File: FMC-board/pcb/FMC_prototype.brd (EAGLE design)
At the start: 76.5 x 69 mm, 71 parts, among them U1 4901, U2 TPS79333, U3 ADN4663, U4 ADN4663, U5 ADN4664, U6 PDS1-S12-S5-S, U8 4901

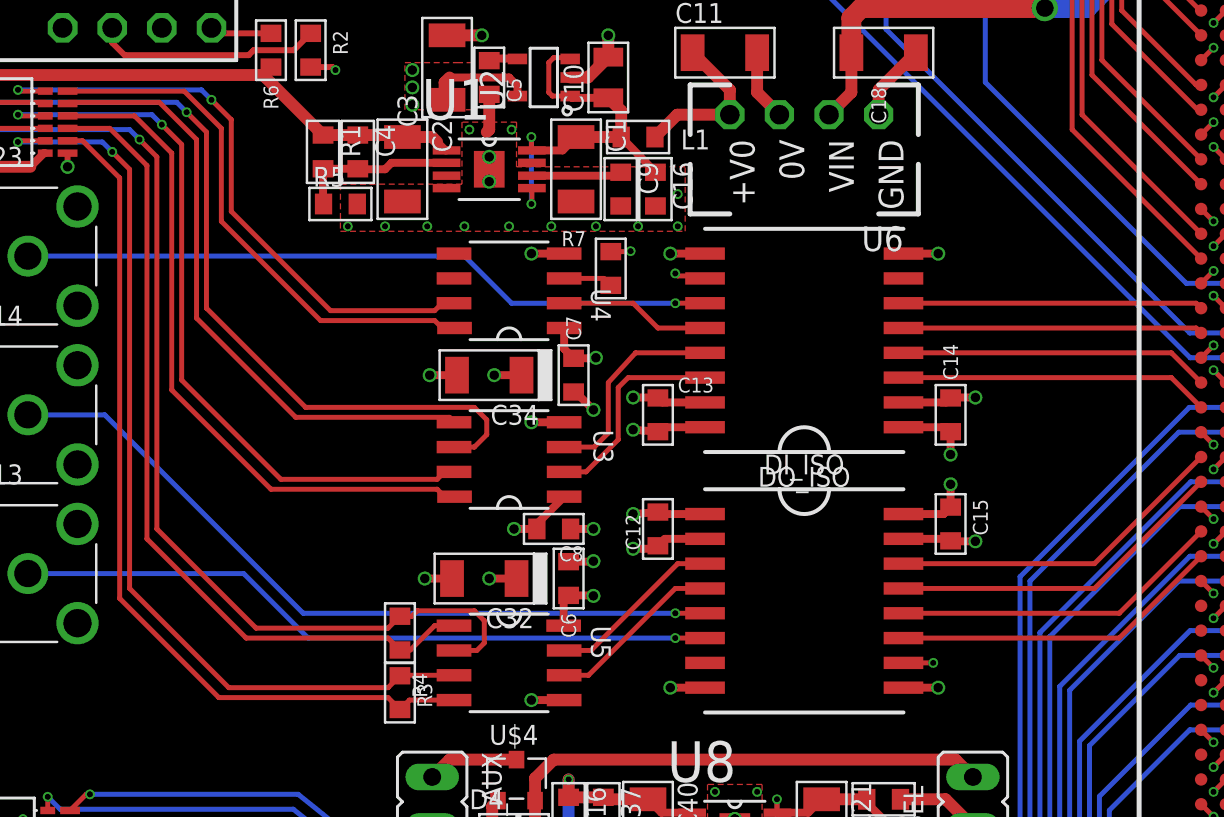
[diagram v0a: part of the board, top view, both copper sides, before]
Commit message: tightened routing a bit & added 3v3 test point
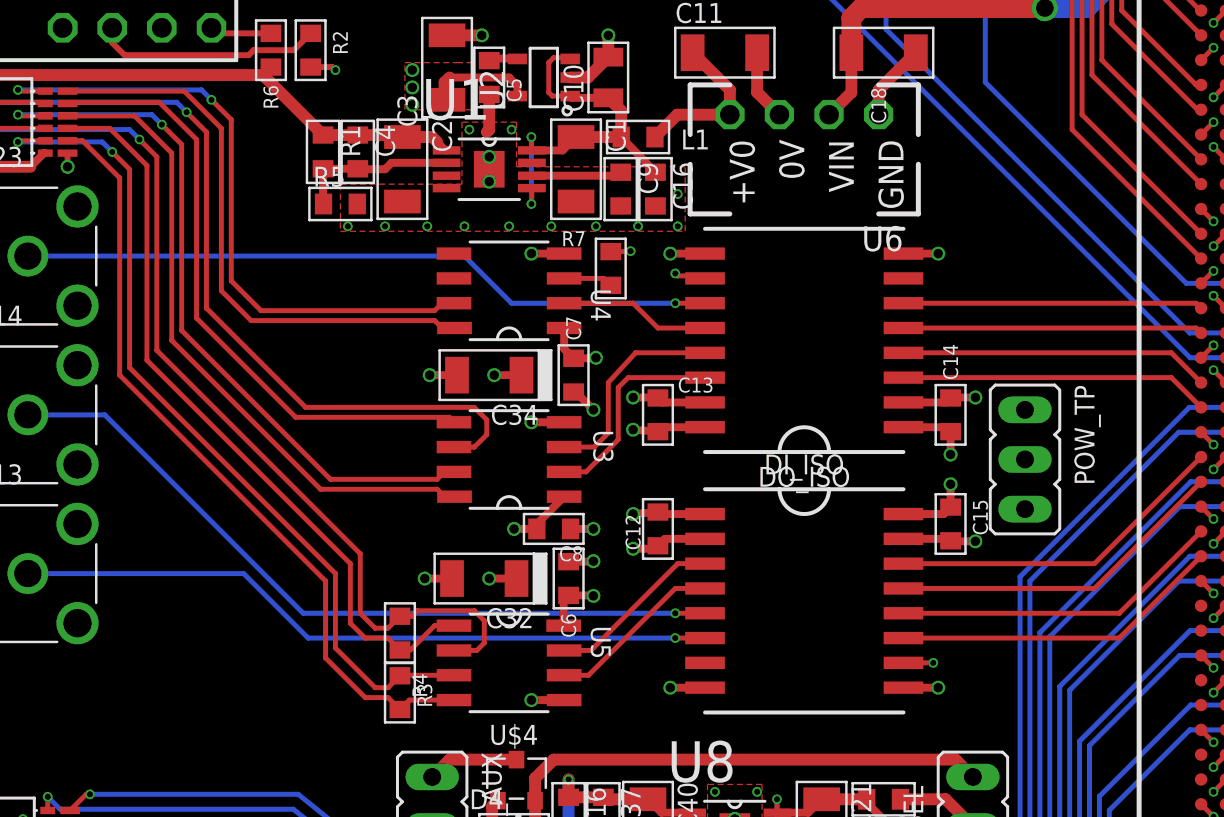
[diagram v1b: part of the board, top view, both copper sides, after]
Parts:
- added POW_TP: (no value), jonnew:JP3
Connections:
- new net N$11: POW_TP.2
- net +3V3: now also POW_TP.1
- net GND: now also POW_TP.3
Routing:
- net MISO2-_ISOLATED: track 44.9 -> 40.5 mm
- net MISO2+_ISOLATED: track 48.4 -> 44.0 mm
- net MISO1+_ISOLATED: track 53.5 -> 50.0 mm
- net MISO1-_ISOLATED: track 42.6 -> 39.0 mm
- net CS+_ISOLATED: track 31.3 -> 33.4 mm
- net CS-_ISOLATED: track 27.6 -> 29.7 mm
- net N$13: track 35.0 -> 33.5 mm
- net N$12: track 38.7 -> 37.2 mm

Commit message: connected FMC mount holes to non-isolated gnd
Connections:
- net GND: now also U$2.BEZ1, U$2.BEZ2
- net GND_ISO: no longer U$2.BEZ1, U$2.BEZ2
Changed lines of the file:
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@@
 <wire x1="3.175" y1="49.3014" x2="2.159" y2="49.3014" width="0.254" layer="16"/>
 <contactref element="POW_TP" pad="3"/>
+<contactref element="U$2" pad="BEZ2"/>
+<contactref element="U$2" pad="BEZ1"/>
 </signal>
 <signal name="MISO1_ISO">
@@
 <contactref element="H14" pad="GND$2"/>
 <contactref element="C11" pad="2"/>
-<contactref element="U$2" pad="BEZ2"/>
-<contactref element="U$2" pad="BEZ1"/>
 <polygon width="0.4064" layer="2" isolate="0.254">
 <vertex x="-67.31" y="13.589"/>
@@
 <wire x1="-30.3784" y1="37.5666" x2="-30.353" y2="37.592" width="0.254" layer="1"/>
 <wire x1="-33.7566" y1="37.465" x2="-35.433" y2="37.465" width="0.4064" layer="1"/>
-<wire x1="-58.674" y1="18.542" x2="-54.6" y2="2.5" width="0" layer="19" extent="1-1"/>
-<wire x1="-54.6" y1="59.05" x2="-54.356" y2="49.022" width="0" layer="19" extent="1-1"/>
 </signal>
 <signal name="+3V6_ISO">

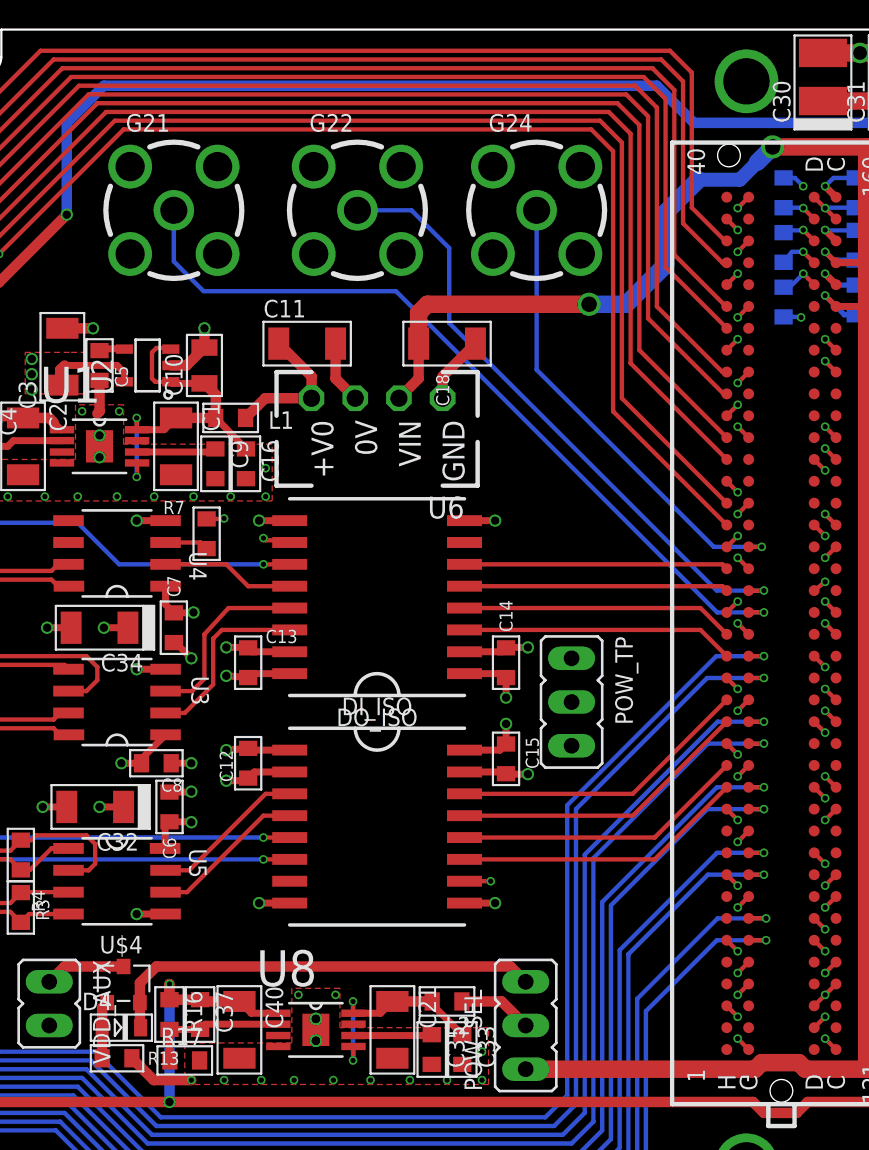
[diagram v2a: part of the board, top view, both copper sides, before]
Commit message: added schottky diodes for FPGA input protection
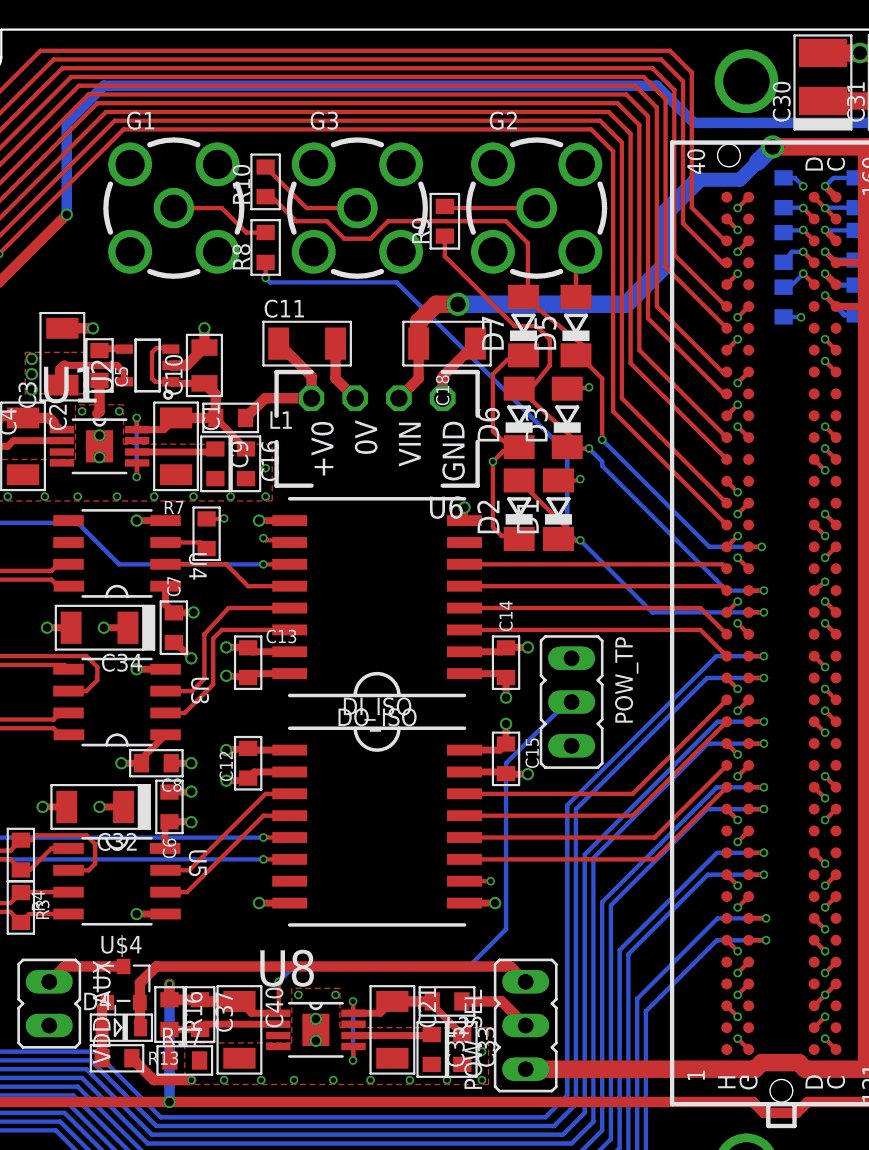
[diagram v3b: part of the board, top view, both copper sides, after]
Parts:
- removed G21, G22, G24: 142-0701, jonnew:SMA_JACK_142-0701-201
- added D1, D2, D3, D5, D6, D7: PMLL4150, diode:SOD80C
- added G1, G2, G3: 142-0701, jonnew:SMA_JACK_142-0701-201
- added R10, R8, R9: 100, jonnew:0603
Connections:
- removed net N$11: POW_TP.2
- new net N$18: G2.CLK, R9.2
- new net N$19: G3.CLK, R10.2
- new net N$2: G1.CLK, R8.2
- net +3V3: now also D2.C, D6.C, D7.C
- net +3V6: now also POW_TP.2
- net G21: now also D1.C, D2.A, R8.1; no longer G21.CLK
- net G22: now also D3.C, D6.A, R9.1; no longer G22.CLK
- net G24: now also D5.C, D7.A, R10.1; no longer G24.CLK
- net GND: now also D1.A, D3.A, D5.A, G1.GND$1, G1.GND$2, G1.GND$3, G1.GND$4, G2.GND$1, G2.GND$2, G2.GND$3, G2.GND$4, G3.GND$1, G3.GND$2, G3.GND$3, G3.GND$4; no longer G21.GND$1, G21.GND$2, G21.GND$3, G21.GND$4, G22.GND$1, G22.GND$2, G22.GND$3, G22.GND$4, G24.GND$1, G24.GND$2, G24.GND$3, G24.GND$4
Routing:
- net +3V6: track 220.3 -> 251.6 mm, vias 4 -> 5
- net G24: track 27.4 -> 43.9 mm, vias 1 -> 2
- net +3V3: track 18.3 -> 34.4 mm, vias 7 -> 8
- net N$19: track 0.00 -> 6.32 mm
- net N$2: track 0.00 -> 5.92 mm
- net N$18: track 0.00 -> 5.38 mm
- net GND: track 90.1 -> 94.9 mm
- net G21: track 46.6 -> 47.9 mm, vias 1 -> 3
- net G22: track 36.2 -> 35.1 mm, vias 1 -> 2

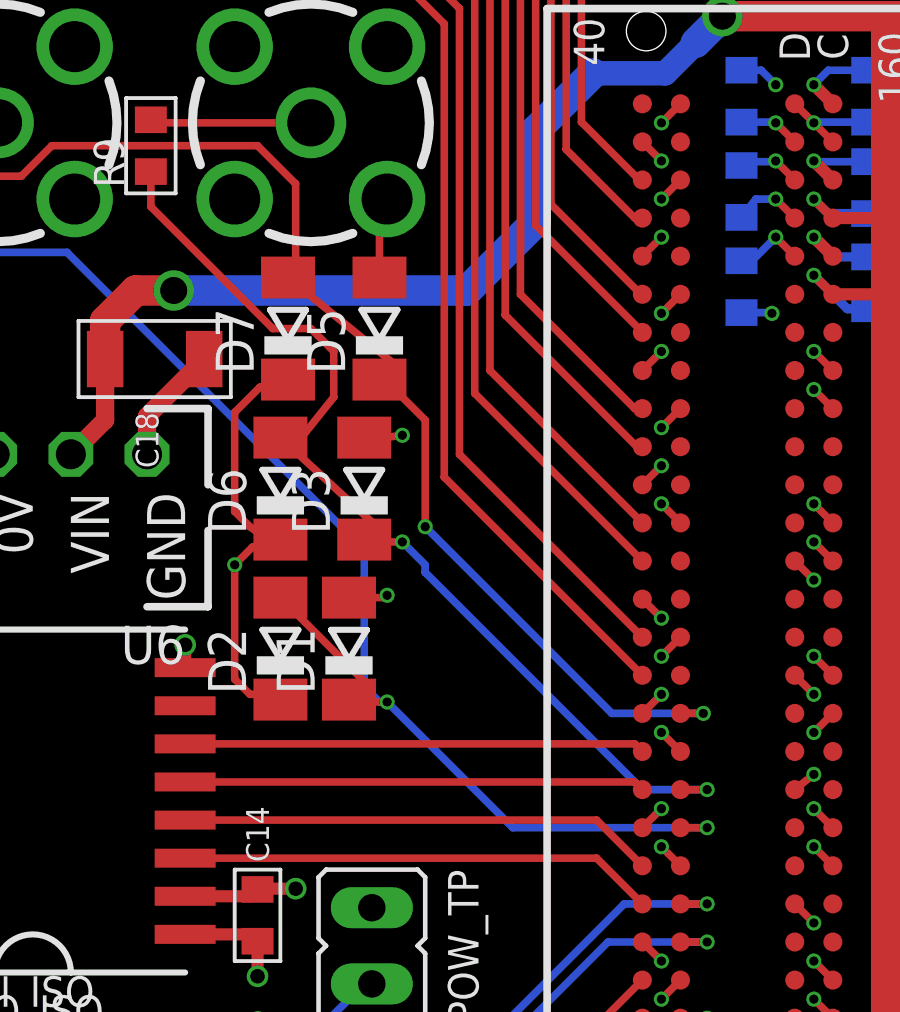
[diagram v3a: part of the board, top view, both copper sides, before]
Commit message: cleaning up diode layout
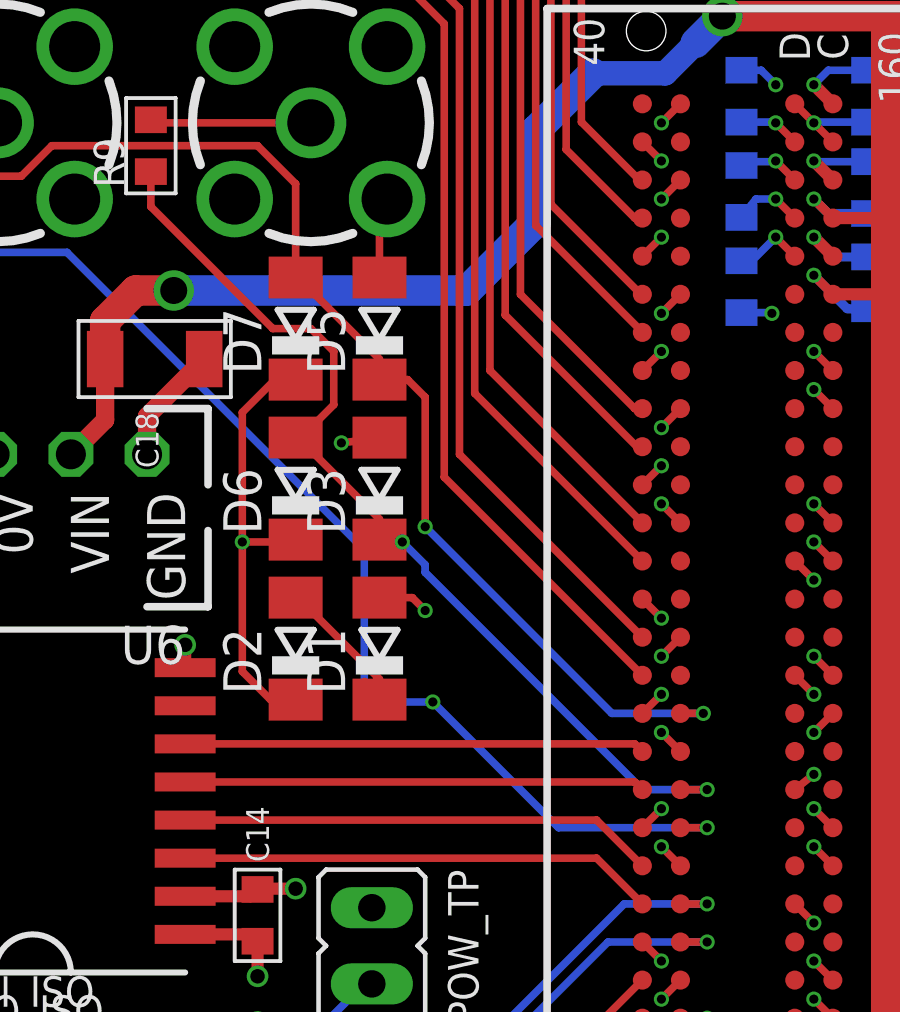
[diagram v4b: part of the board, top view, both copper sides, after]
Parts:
- moved D1 1.02 mm to (-9.91, 38.1)
- moved D2 0.51 mm to (-12.7, 38.1)
- moved D6 0.51 mm to (-12.7, 43.4)
- moved D3 0.51 mm to (-9.91, 43.4)
- moved D7 0.25 mm to (-12.7, 48.8)
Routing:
- net GND: track 94.9 -> 98.3 mm
- net G22: track 35.1 -> 33.1 mm
- net G21: track 47.9 -> 46.7 mm
- net G24: track 43.9 -> 44.9 mm
- net +3V3: track 34.4 -> 33.5 mm

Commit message: some labelling
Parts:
- moved U$1 88.0 mm to (24.6, 55.9)
- moved U$16 71.7 mm to (26.2, 43.6)
- renumbered A_ISOLATED to C_ISOLATED
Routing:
- net G21: track 46.7 -> 47.2 mm
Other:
- board text added: "+3v3"
- board text added: "+3v6"
- board text added: "C"
- board text removed: "5V non- isolated"
- board text removed: "5v"
- board text removed: "TP"
- board text removed: "TP4"
- board text removed: "TP5"
- board text removed: "TP6"
- board text removed: "TP7"
- board text removed: "TP8"
- board text removed: "fpga12>5V DCDC"
- board text removed: "jack"

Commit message: Overvoltage protection and silkscreen cleanup
- Finished adding Schottky protection rectifiers to all SMA inputs,
  included isolated lines.
- Left the Bezel connector floating, since this is supposed to be
  galvanically isolated from the FPGA ground. Eventually, we will
  probably tie to GND_ISO, but its more trouble than its worth now
- Cleaned up silkscreen
- Started BOM
- Added missing datasheets.
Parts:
- added D10, D11, D12, D13, D8, D9: STPS0560Z, jonnew:SOD123
- added R11, R12, R14: 100, jonnew:0603
- C17, C20, C24, C27, C29: value 100n -> 100nF
- D1, D2, D3, D5, D6, D7: value PMLL4150 -> STPS0560Z; device diode:SOD80C -> jonnew:SOD123
- moved G1 0.25 mm to (-33.5, 55.6)
- moved G3 0.25 mm to (-22.9, 55.6)
- moved R10 0.25 mm to (-28.2, 57.1)
- moved R8 0.25 mm to (-28.2, 53.3)
- turned D1 to 270 degrees
- turned D2 to 270 degrees
- turned D3 to 270 degrees
- turned D5 to 270 degrees
- turned D6 to 270 degrees
- turned D7 to 270 degrees
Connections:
- new net N$11: H23.CLK, R11.2
- new net N$14: H14.CLK, R12.2
- new net N$17: H13.CLK, R14.2
- net +3V3_ISO: now also D12.C, D13.C, D8.C
- net GND: no longer U$2.BEZ1, U$2.BEZ2
- net GND_ISO: now also D10.A, D11.A, D9.A
- net H13_ISO: now also D11.C, D13.A, R14.1; no longer H13.CLK
- net H14_ISO: now also D10.C, D12.A, R12.1; no longer H14.CLK
- net H23_ISO: now also D8.A, D9.C, R11.1; no longer H23.CLK
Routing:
- net +3V3: track 33.5 -> 21.8 mm, vias 8 -> 10
- net H13_ISO: track 36.0 -> 28.0 mm
- net H23_ISO: track 35.7 -> 29.3 mm
- net N$17: track 0.00 -> 4.72 mm
- net N$14: track 0.00 -> 4.72 mm
- net N$11: track 0.00 -> 4.72 mm
- net GND_ISO: track 35.5 -> 39.3 mm, vias 30 -> 33
- net +3V3_ISO: track 28.6 -> 32.3 mm, vias 12 -> 15
- net G21: track 47.2 -> 43.8 mm, vias 3 -> 4
- net GND: track 98.3 -> 95.4 mm, vias 84 -> 85
- net H14_ISO: track 38.9 -> 36.2 mm
- net G24: track 44.9 -> 43.4 mm
- net G22: track 33.4 -> 32.2 mm
